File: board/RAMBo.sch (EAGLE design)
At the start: 266 parts, among them Q1 PSMN7R0-60YS, Q2 PSMN7R0-60YS, Q3 PSMN7R0-60YS, Q4 IRLML6346TRPBF, Q5 PSMN7R0-60YS, Q8 IRLML6346TRPBF, U1 ATMEGA32U2-MUR, U10 ADUM7441, U2 ATMEGA2560-16AU, U3 LM22675, U4 AD5206, U5 A4982, U6 A4982, U7 A4982, U8 A4982, U9 A4982, X1 C-GRID-02-70543, X10 C-GRID-04-70543, X11 MSTBV10, X12 SPI, X13 EXT-2, X14 C-GRID-04-70543, X15 C-GRID-04-70543, X16 32u2 EXT, X17 3x2M, X18 3x2M, X2 USB B-TH, X20 MX1, X21 C-GRID-03-70543, X22 C-GRID-03-70543, X23 C-GRID-03-70543, X24 C-GRID-03-70543, X25 C-GRID-03-70543, X26 C-GRID-03-70543, X27 C-GRID-02-70543, X28 C-GRID-02-70543, X29 C-GRID-02-70543, X3 C-GRID-02-70543, X30 C-GRID-02-70543, X31 MX2, X32 MX3, X33 MSTBA6, X34 PWM_EXT, X39 M05X2PTH, X4 C-GRID-04-70543, X40 Analog, X5 C-GRID-02-70543, X6 C-GRID-04-70543, X7 C-GRID-04-70543, X8 C-GRID-04-70543, X9 C-GRID-02-70543, Y1 16MHz KX-7, Y2 16MHz KX-7

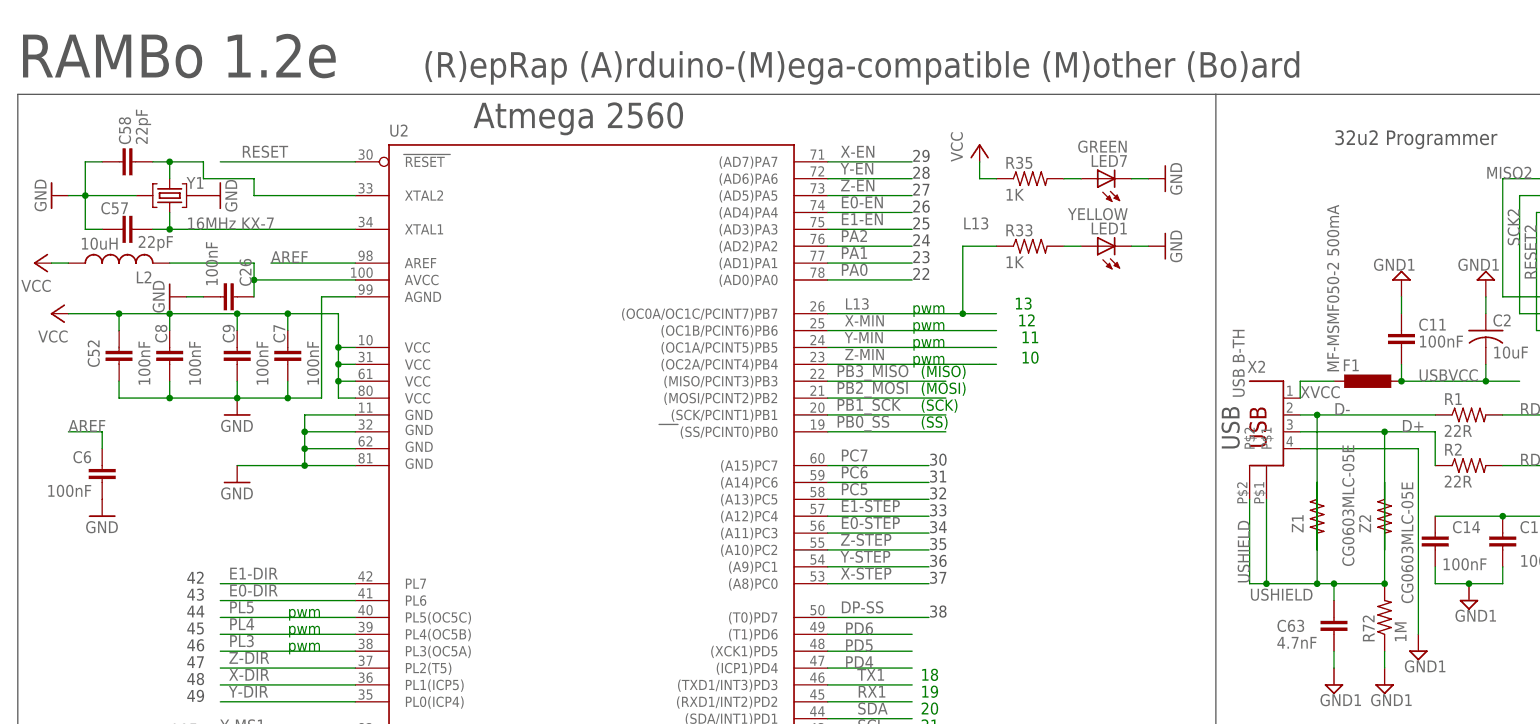
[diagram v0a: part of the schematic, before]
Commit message: fix rotated varistors on schematic, no EDC
increment schematic label to 1.2g
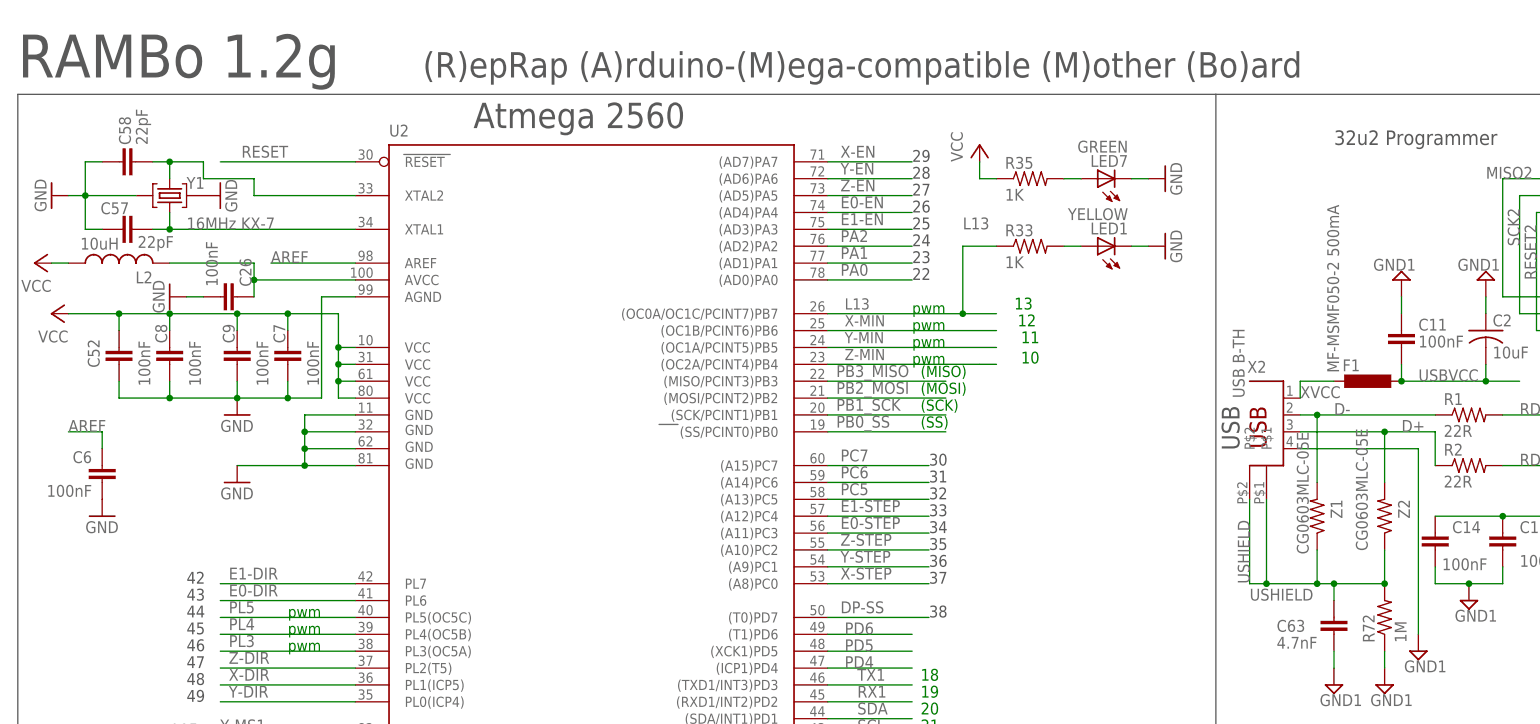
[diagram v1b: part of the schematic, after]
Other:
- note added: "RAMBo 1.2g"
- note removed: "RAMBo 1.2e"
- moved on the sheet: Z1, Z2
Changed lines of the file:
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@@
 <text x="308.61" y="44.45" size="3.81" layer="97">E0</text>
 <text x="419.1" y="45.72" size="3.81" layer="97">E1</text>
-<text x="251.46" y="330.2" size="6.4516" layer="97">RAMBo 1.2e</text>
+<text x="251.46" y="330.2" size="6.4516" layer="97">RAMBo 1.2g</text>
 <text x="518.16" y="322.58" size="3.81" layer="97">Atmega 32u2 USB</text>
 <text x="723.9" y="157.48" size="3.81" layer="97">I2C Expansion</text>
@@
 <instance part="U1" gate="G$1" x="541.02" y="266.7"/>
 <instance part="X17" gate="A" x="487.68" y="312.42"/>
-<instance part="Z1" gate="G$1" x="447.04" y="264.16" smashed="yes" rot="MR270">
-<attribute name="NAME" x="443.23" y="261.62" size="1.778" layer="95" rot="MR90"/>
-<attribute name="VALUE" x="450.85" y="256.54" size="1.778" layer="96" rot="MR90"/>
-</instance>
-<instance part="Z2" gate="G$1" x="457.2" y="264.16" smashed="yes" rot="MR270">
-<attribute name="NAME" x="453.39" y="261.62" size="1.778" layer="95" rot="MR90"/>
-<attribute name="VALUE" x="459.74" y="250.952" size="1.778" layer="96" rot="MR90"/>
+<instance part="Z1" gate="G$1" x="447.04" y="264.16" smashed="yes" rot="MR90">
+<attribute name="NAME" x="450.85" y="266.7" size="1.778" layer="95" rot="MR270"/>
+<attribute name="VALUE" x="445.77" y="276.86" size="1.778" layer="96" rot="MR270"/>
+</instance>
+<instance part="Z2" gate="G$1" x="457.2" y="264.16" smashed="yes" rot="MR90">
+<attribute name="NAME" x="461.01" y="266.7" size="1.778" layer="95" rot="MR270"/>
+<attribute name="VALUE" x="454.66" y="277.368" size="1.778" layer="96" rot="MR270"/>
 </instance>
 <instance part="RN5" gate="A" x="622.3" y="231.14" rot="R180"/>
@@
 <wire x1="444.5" y1="279.4" x2="447.04" y2="279.4" width="0.1524" layer="91"/>
 <wire x1="447.04" y1="279.4" x2="464.82" y2="279.4" width="0.1524" layer="91"/>
-<wire x1="447.04" y1="259.08" x2="447.04" y2="279.4" width="0.1524" layer="91"/>
+<wire x1="447.04" y1="269.24" x2="447.04" y2="279.4" width="0.1524" layer="91"/>
 <junction x="447.04" y="279.4"/>
 <label x="449.58" y="279.4" size="1.778" layer="95"/>
@@
 <wire x1="464.82" y1="276.86" x2="457.2" y2="276.86" width="0.1524" layer="91"/>
 <wire x1="457.2" y1="276.86" x2="444.5" y2="276.86" width="0.1524" layer="91"/>
-<wire x1="457.2" y1="259.08" x2="457.2" y2="276.86" width="0.1524" layer="91"/>
+<wire x1="457.2" y1="269.24" x2="457.2" y2="276.86" width="0.1524" layer="91"/>
 <wire x1="464.82" y1="271.78" x2="464.82" y2="276.86" width="0.1524" layer="91"/>
 <junction x="457.2" y="276.86"/>
@@
 <segment>
 <wire x1="436.88" y1="254" x2="436.88" y2="266.7" width="0.1524" layer="91"/>
-<wire x1="457.2" y1="269.24" x2="457.2" y2="254" width="0.1524" layer="91"/>
+<wire x1="457.2" y1="259.08" x2="457.2" y2="254" width="0.1524" layer="91"/>
 <wire x1="447.04" y1="254" x2="449.58" y2="254" width="0.1524" layer="91"/>
 <wire x1="449.58" y1="254" x2="457.2" y2="254" width="0.1524" layer="91"/>
-<wire x1="447.04" y1="269.24" x2="447.04" y2="254" width="0.1524" layer="91"/>
+<wire x1="447.04" y1="259.08" x2="447.04" y2="254" width="0.1524" layer="91"/>
 <wire x1="439.42" y1="266.7" x2="439.42" y2="254" width="0.1524" layer="91"/>
 <wire x1="439.42" y1="254" x2="447.04" y2="254" width="0.1524" layer="91"/>
